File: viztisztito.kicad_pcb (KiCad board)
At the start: 2 copper layers, 110 x 102 mm, 77 parts, among them P1 BOARD_CONN, Q1 BC850, U1 VTX-214-010-205, U2 LTV-847, U3 ACS722, U4 MCP3004, U5 TC77

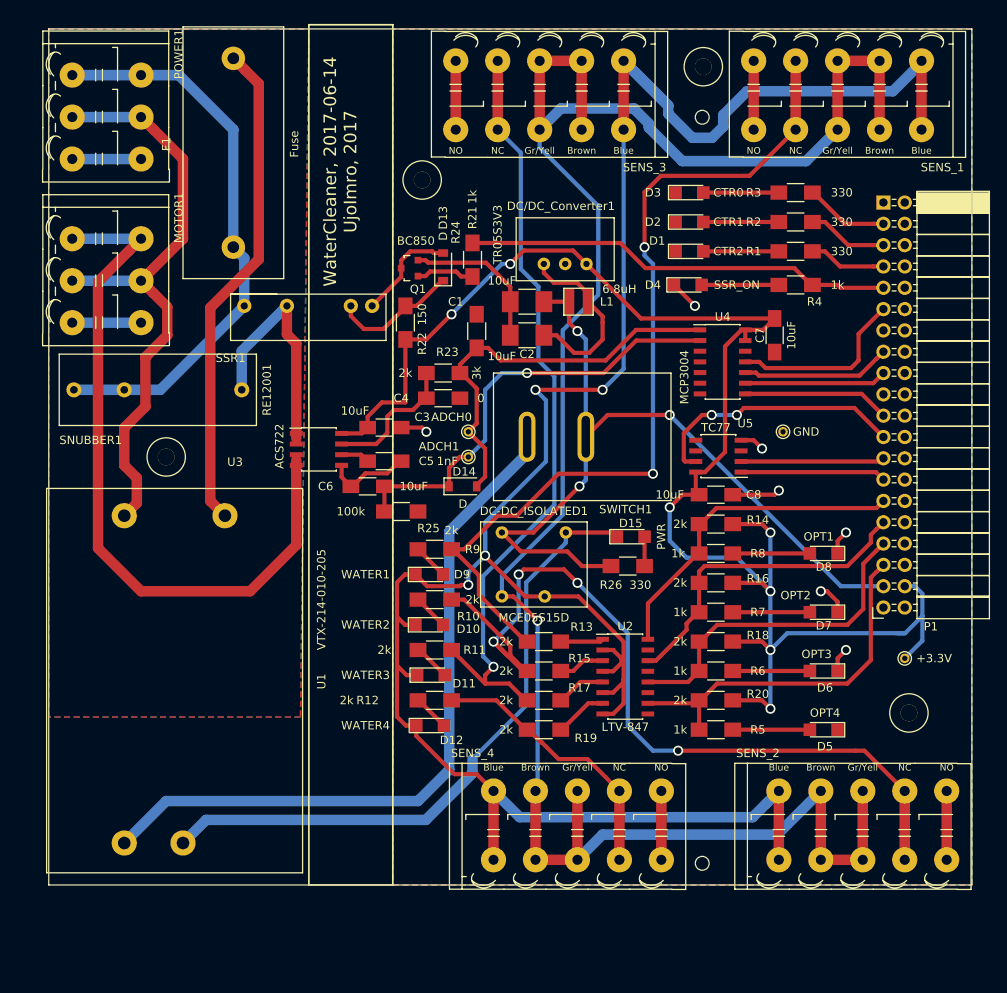
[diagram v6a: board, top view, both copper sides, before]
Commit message: power supply mirrored
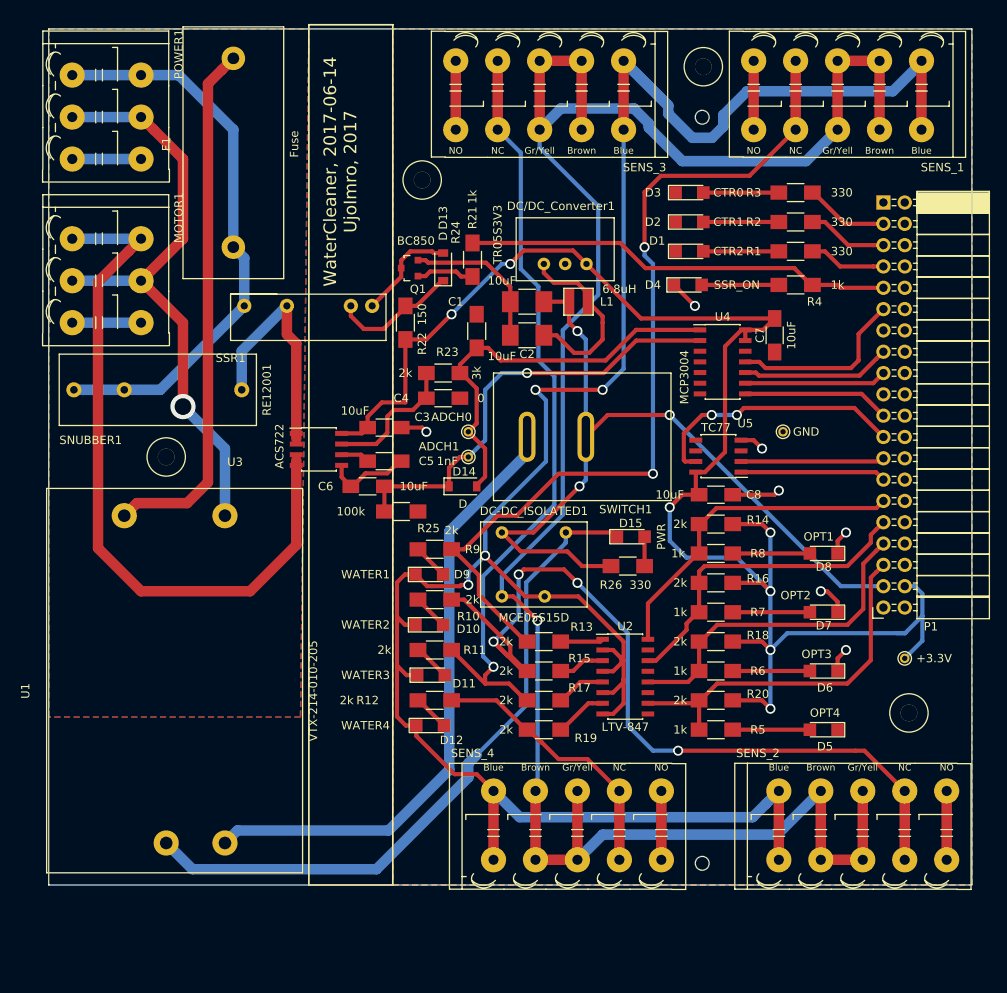
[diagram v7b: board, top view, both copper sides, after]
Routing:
- net Net-(SWITCH1-Pad1): track 86.3 -> 74.3 mm
- net GND: track 130.8 -> 136.1 mm
- net Net-(F1-Pad1): track 58.9 -> 63.4 mm
- net 230V_NEUTRAL: track 72.7 -> 72.2 mm, vias 0 -> 1
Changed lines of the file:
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@@
     (thickness 1.6)
     (drawings 29)
-    (tracks 561)
+    (tracks 558)
     (zones 0)
     (modules 77)
@@
     (add_net /T_SCK)
     (add_net /T_SIO)
-    (add_net GND)
     (add_net "Net-(C2-Pad1)")
     (add_net "Net-(C4-Pad1)")
@@
     (add_net 230V_GND)
     (add_net 230V_NEUTRAL)
+    (add_net GND)
     (add_net ISOLATED_GND)
     (add_net "Net-(F1-Pad1)")
@@
       (net 1 +5V))
   )
-  (module water:VTX-214-010-205 (layer F.Cu)
-    (at 54.25 77.75 270)
-    (fp_text reference U1 (at 23 -2.25 270) (layer F.SilkS)
-      (effects (font (size 1 1) (thickness 0.15)))
-    )
-    (fp_text value VTX-214-010-205 (at 13.25 -2.25 450) (layer F.SilkS)
-      (effects (font (size 1 1) (thickness 0.15)))
-    )
-    (fp_line (start 0 30.5) (end 0 0) (layer F.SilkS) (width 0.15))
-    (fp_line (start 45.8 30.5) (end 0 30.5) (layer F.SilkS) (width 0.15))
-    (fp_line (start 45.8 0) (end 45.8 30.5) (layer F.SilkS) (width 0.15))
-    (fp_line (start 0 0) (end 45.8 0) (layer F.SilkS) (width 0.15))
-    (pad 1 thru_hole circle (at 3.25 9.25 270) (size 3 3) (drill 1.5) (layers *.Cu *.Mask)
-      (net 25 "Net-(F1-Pad1)"))
-    (pad 2 thru_hole circle (at 3.25 21.25 270) (size 3 3) (drill 1.5) (layers *.Cu *.Mask)
-      (net 28 230V_NEUTRAL))
-    (pad 3 thru_hole circle (at 42.25 21.25 270) (size 3 3) (drill 1.5) (layers *.Cu *.Mask)
-      (net 59 "Net-(SWITCH1-Pad1)"))
-    (pad 4 thru_hole circle (at 42.25 14.25 270) (size 3 3) (drill 1.5) (layers *.Cu *.Mask)
-      (net 2 GND))
-  )
   (module Housings_SOIC:SOIC-16_3.9x9.9mm_Pitch1.27mm (layer F.Cu)
     (at 92.7 100.175)
@@
       (net 26 230V_AC+))
   )
+  (module water:VTX-214-010-205 (layer F.Cu)
+    (at 54.25 77.75 270)
+    (fp_text reference U1 (at 24.13 33.02 270) (layer F.SilkS)
+      (effects (font (size 1 1) (thickness 0.15)))
+    )
+    (fp_text value VTX-214-010-205 (at 24.13 -1.27 270) (layer F.SilkS)
+      (effects (font (size 1 1) (thickness 0.15)))
+    )
+    (fp_line (start 0 30.5) (end 0 0) (layer F.SilkS) (width 0.15))
+    (fp_line (start 45.8 30.5) (end 0 30.5) (layer F.SilkS) (width 0.15))
+    (fp_line (start 45.8 0) (end 45.8 30.5) (layer F.SilkS) (width 0.15))
+    (fp_line (start 0 0) (end 45.8 0) (layer F.SilkS) (width 0.15))
+    (pad 2 thru_hole circle (at 3.25 9.25 270) (size 3 3) (drill 1.5) (layers *.Cu *.Mask)
+      (net 28 230V_NEUTRAL))
+    (pad 1 thru_hole circle (at 3.25 21.25 270) (size 3 3) (drill 1.5) (layers *.Cu *.Mask)
+      (net 25 "Net-(F1-Pad1)"))
+    (pad 4 thru_hole circle (at 42.25 16.25 270) (size 3 3) (drill 1.5) (layers *.Cu *.Mask)
+      (net 2 GND))
+    (pad 3 thru_hole circle (at 42.25 9.25 270) (size 3 3) (drill 1.5) (layers *.Cu *.Mask)
+      (net 59 "Net-(SWITCH1-Pad1)"))
+  )
   (gr_text "WaterCleaner, 2017-06-14\nUjoImro, 2017" (at 58.75 40 90) (layer F.SilkS)
     (effects (font (size 1.5 1.5) (thickness 0.3)))
@@
   (segment (start 90.6 69) (end 88 71.6) (width 0.5) (layer F.Cu) (net 1))
   (segment (start 86 55.5) (end 83 55.5) (width 0.5) (layer F.Cu) (net 1))
-  (segment (start 74.5 110) (end 80.900009 103.599991) (width 0.5) (layer B.Cu) (net 2))
+  (segment (start 74.5 110) (end 75 109.5) (width 0.5) (layer B.Cu) (net 2))
+  (segment (start 75 109.5) (end 80.900009 103.599991) (width 0.5) (layer B.Cu) (net 2))
+  (segment (start 74 110.5) (end 75 109.5) (width 1.25) (layer B.Cu) (net 2))
+  (segment (start 74 112.181994) (end 74 110.5) (width 1.25) (layer B.Cu) (net 2))
+  (segment (start 38 120) (end 41.125001 123.125001) (width 1.25) (layer B.Cu) (net 2))
+  (segment (start 41.125001 123.125001) (end 63.056993 123.125001) (width 1.25) (layer B.Cu) (net 2))
+  (segment (start 63.056993 123.125001) (end 74 112.181994) (width 1.25) (layer B.Cu) (net 2))
   (segment (start 80.900009 103.599991) (end 80.900009 88.949993) (width 0.5) (layer B.Cu) (net 2))
   (segment (start 80.900009 88.949993) (end 85.62 84.230002) (width 0.5) (layer B.Cu) (net 2))
   (segment (start 85.62 84.230002) (end 85.62 84.06066) (width 0.5) (layer B.Cu) (net 2))
   (segment (start 85.62 84.06066) (end 85.62 83) (width 0.5) (layer B.Cu) (net 2))
-  (segment (start 74.5 111.681994) (end 74.5 110) (width 1.25) (layer B.Cu) (net 2))
-  (segment (start 40 120) (end 42.74999 117.25001) (width 1.25) (layer B.Cu) (net 2))
-  (segment (start 42.74999 117.25001) (end 68.931985 117.250009) (width 1.25) (layer B.Cu) (net 2))
-  (segment (start 68.931985 117.250009) (end 74.5 111.681994) (width 1.25) (layer B.Cu) (net 2))
   (segment (start 85.62 83) (end 91.2 83) (width 0.5) (layer F.Cu) (net 2))
   (segment (start 91.2 83) (end 91.7 83.5) (width 0.5) (layer F.Cu) (net 2))
@@
   (segment (start 87.5 35) (end 87.5 26.8) (width 1.25) (layer F.Cu) (net 24))
   (segment (start 82.5 35) (end 82.5 26.8) (width 1.25) (layer F.Cu) (net 24))
-  (segment (start 45 81) (end 43.25001 79.25001) (width 1.25) (layer F.Cu) (net 25))
-  (segment (start 43.25001 79.25001) (end 43.25001 56.226992) (width 1.25) (layer F.Cu) (net 25))
-  (segment (start 43.25001 56.226992) (end 49.025001 50.452001) (width 1.25) (layer F.Cu) (net 25))
-  (segment (start 49.025001 50.452001) (end 49.025001 29.525001) (width 1.25) (layer F.Cu) (net 25))
-  (segment (start 49.025001 29.525001) (end 47.399999 27.899999) (width 1.25) (layer F.Cu) (net 25))
-  (segment (start 47.399999 27.899999) (end 46 26.5) (width 1.25) (layer F.Cu) (net 25))
+  (segment (start 33 81) (end 34.499999 79.500001) (width 1.25) (layer F.Cu) (net 25))
+  (segment (start 34.499999 79.500001) (end 40.499999 79.500001) (width 1.25) (layer F.Cu) (net 25))
+  (segment (start 42.974999 77.025001) (end 42.974999 29.525001) (width 1.25) (layer F.Cu) (net 25))
+  (segment (start 40.499999 79.500001) (end 42.974999 77.025001) (width 1.25) (layer F.Cu) (net 25))
+  (segment (start 42.974999 29.525001) (end 44.600001 27.899999) (width 1.25) (layer F.Cu) (net 25))
+  (segment (start 44.600001 27.899999) (end 46 26.5) (width 1.25) (layer F.Cu) (net 25))
   (segment (start 33 66) (end 37.3 66) (width 1.25) (layer B.Cu) (net 26))
   (segment (start 37.3 66) (end 47.3 56) (width 1.25) (layer B.Cu) (net 26))
@@
   (segment (start 26.80126 58) (end 35.00126 58) (width 1.25) (layer B.Cu) (net 27))
   (segment (start 26.80126 38.49936) (end 35.00126 38.49936) (width 1.25) (layer B.Cu) (net 27))
-  (segment (start 35.525001 68) (end 35.525001 62.101261) (width 1.25) (layer F.Cu) (net 28))
-  (segment (start 33 75) (end 33 70.525001) (width 1.25) (layer F.Cu) (net 28))
-  (segment (start 33 70.525001) (end 35.525001 68) (width 1.25) (layer F.Cu) (net 28))
-  (segment (start 34.499999 76.499999) (end 33 75) (width 1.25) (layer F.Cu) (net 28))
-  (segment (start 33 81) (end 34.499999 79.500001) (width 1.25) (layer F.Cu) (net 28))
-  (segment (start 34.499999 79.500001) (end 34.499999 76.499999) (width 1.25) (layer F.Cu) (net 28))
-  (segment (start 35.525001 62.101261) (end 38.126261 59.500001) (width 1.25) (layer F.Cu) (net 28))
-  (segment (start 36.501259 54.499999) (end 35.00126 53) (width 1.25) (layer F.Cu) (net 28))
-  (segment (start 38.126261 59.500001) (end 38.126261 56.125001) (width 1.25) (layer F.Cu) (net 28))
-  (segment (start 38.126261 56.125001) (end 36.501259 54.499999) (width 1.25) (layer F.Cu) (net 28))
+  (segment (start 40 68) (end 40 57.99874) (width 1.25) (layer F.Cu) (net 28))
+  (segment (start 40 57.99874) (end 35.00126 53) (width 1.25) (layer F.Cu) (net 28))
+  (segment (start 45 81) (end 45 73) (width 1.25) (layer B.Cu) (net 28))
+  (segment (start 45 73) (end 40 68) (width 1.25) (layer B.Cu) (net 28))
+  (via (at 40 68) (size 3) (drill 2) (layers F.Cu B.Cu) (net 28))
   (segment (start 35.00126 53) (end 40 48.00126) (width 1.25) (layer F.Cu) (net 28))
   (segment (start 40 48.00126) (end 40 38.4981) (width 1.25) (layer F.Cu) (net 28))
@@
   (segment (start 53.5 60.5) (end 53.5 71.804999) (width 1.25) (layer F.Cu) (net 58))
   (segment (start 52.38 56) (end 52.38 59.38) (width 1.25) (layer F.Cu) (net 58))
-  (segment (start 68 115) (end 71.724989 111.275011) (width 1.25) (layer B.Cu) (net 59))
-  (segment (start 38 115) (end 68 115) (width 1.25) (layer B.Cu) (net 59))
-  (segment (start 33 120) (end 38 115) (width 1.25) (layer B.Cu) (net 59))
+  (segment (start 45 120) (end 46.499999 118.500001) (width 1.25) (layer B.Cu) (net 59))
+  (segment (start 46.499999 118.500001) (end 64.499999 118.500001) (width 1.25) (layer B.Cu) (net 59))
+  (segment (start 64.499999 118.500001) (end 71.724989 111.275011) (width 1.25) (layer B.Cu) (net 59))
   (segment (start 71.724989 111.275011) (end 71.724989 82.875011) (width 1.25) (layer B.Cu) (net 59))
   (segment (start 71.724989 82.875011) (end 81 73.6) (width 1.25) (layer B.Cu) (net 59))
